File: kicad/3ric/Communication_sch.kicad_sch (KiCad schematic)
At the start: 15 parts, among them J4_ACIA 6502-library_65C51N

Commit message: cleaning up of the schematic
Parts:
- H1_LEVEL_SHIFT1: renamed from H1_LEVEL_SHIFT; footprint (none) -> Package_SO:ETSSOP-20-1EP_4.4x6.5mm_P0.65mm_EP3x4.2mm
- Y_SNES_1, Y_SNES_2: footprint Nintendo:SNES_Controller_Socket -> snes:SNES_Controller_Socket
- renumbered H2_ACIA_CLK to H2_ACIA_CLK1, I1_VIA to I1_VIA1, J4_ACIA to J4_ACIA1, RM to RM1, Y_DEVICE_PORT to Y_DEVICE_PORT1, Y_MICRO_SD to Y_MICRO_SD1, Y_PS2_KB to Y_PS2_KB1, Y_PS2_MOUSE to Y_PS2_MOUSE1, Y_SERIAL_PINS to Y_SERIAL_PINS1
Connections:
- net V3.3 is gone; now on net 3.3V: Y_DEVICE_PORT1.20 (Pin_20)
- net ~{CS_IO6} is gone; now on net R~{W}: Y_DEVICE_PORT1.22 (Pin_22)
- net GND: no longer J4_ACIA1.9 (~{CTS})
- net ~{CTS}: now also J4_ACIA1.9 (~{CTS})
- net ~{RTS}: now also J4_ACIA1.8 (~{RTS})
- net VIA1_PA5: no longer names the net of I1_VIA1.7 (PA5)
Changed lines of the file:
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@@
 	)
 	(no_connect
+		(at 139.7 63.5)
+	)
+	(no_connect
 		(at 41.91 115.57)
 	)
@@
 	)
 	(no_connect
-		(at 67.31 125.73)
-	)
-	(no_connect
 		(at 97.79 68.58)
 	)
@@
 		)
 	)
+	(global_label "R~{W}"
+		(shape input)
+		(at 124.46 142.24 0)
+		(fields_autoplaced yes)
+		(effects
+			(font
+				(size 1.27 1.27)
+			)
+			(justify left)
+		)
+		(property "Intersheetrefs" "${INTERSHEET_REFS}"
+			(at 154.94 252.73 0)
+			(effects
+				(font
+					(size 1.27 1.27)
+				)
+				(justify right)
+				(hide yes)
+			)
+		)
+	)
 	(global_label "CA0"
 		(shape input)
@@
 		)
 	)
-	(global_label "GND"
-		(shape input)
-		(at 67.31 123.19 0)
-		(fields_autoplaced yes)
-		(effects
-			(font
-				(size 0.9906 0.9906)
-			)
-			(justify left)
-		)
-		(property "Intersheetrefs" "${INTERSHEET_REFS}"
-			(at -53.34 46.99 0)
-			(effects
-				(font
-					(size 1.27 1.27)
-				)
-				(hide yes)
-			)
-		)
-	)
 	(global_label "~{IRQ_VIA1}"
 		(shape input)
@@
 		)
 	)
-	(global_label "~{CS_IO6}"
-		(shape input)
-		(at 124.46 142.24 0)
-		(fields_autoplaced yes)
-		(effects
-			(font
-				(size 1.27 1.27)
-			)
-			(justify left)
-		)
-		(property "Intersheetrefs" "${INTERSHEET_REFS}"
-			(at 134.0371 142.24 0)
-			(effects
-				(font
-					(size 1.27 1.27)
-				)
-				(justify left)
-				(hide yes)
-			)
-		)
-	)
 	(global_label "CLK_MOUSE"
 		(shape output)
@@
 		)
 	)
+	(global_label "3.3V"
+		(shape input)
+		(at 124.46 139.7 0)
+		(fields_autoplaced yes)
+		(effects
+			(font
+				(size 0.9906 0.9906)
+			)
+			(justify left)
+		)
+		(property "Intersheetrefs" "${INTERSHEET_REFS}"
+			(at 129.5498 139.6381 0)
+			(effects
+				(font
+					(size 0.9906 0.9906)
+				)
+				(justify left)
+				(hide yes)
+			)
+		)
+	)
 	(global_label "DATA_MOUSE"
 		(shape output)
@@
 		)
 	)
-	(global_label "V3.3"
-		(shape input)
-		(at 124.46 139.7 0)
-		(fields_autoplaced yes)
-		(effects
-			(font
-				(size 0.9906 0.9906)
-			)
-			(justify left)
-		)
-		(property "Intersheetrefs" "${INTERSHEET_REFS}"
-			(at 129.5498 139.6381 0)
-			(effects
-				(font
-					(size 0.9906 0.9906)
-				)
-				(justify left)
-				(hide yes)
-			)
-		)
-	)
 	(global_label "CA7"
 		(shape input)
@@
 		)
 	)
+	(global_label "~{RTS}"
+		(shape input)
+		(at 67.31 125.73 0)
+		(fields_autoplaced yes)
+		(effects
+			(font
+				(size 0.9906 0.9906)
+			)
+			(justify left)
+		)
+		(property "Intersheetrefs" "${INTERSHEET_REFS}"
+			(at 196.85 2.54 0)
+			(effects
+				(font
+					(size 1.27 1.27)
+				)
+				(justify left)
+				(hide yes)
+			)
+		)
+	)
 	(global_label "CD2"
 		(shape input)
@@
 		)
 	)
+	(global_label "~{CTS}"
+		(shape input)
+		(at 67.31 123.19 0)
+		(fields_autoplaced yes)
+		(effects
+			(font
+				(size 0.9906 0.9906)
+			)
+			(justify left)
+		)
+		(property "Intersheetrefs" "${INTERSHEET_REFS}"
+			(at -74.93 0 0)
+			(effects
+				(font
+					(size 1.27 1.27)
+				)
+				(hide yes)
+			)
+		)
+	)
 	(global_label "CD3"
 		(shape input)
@@
 		)
 	)
-	(global_label "VIA1_PA5"
-		(shape input)
-		(at 139.7 63.5 180)
-		(fields_autoplaced yes)
-		(effects
-			(font
-				(size 0.9906 0.9906)
-			)
-			(justify right)
-		)
-		(property "Intersheetrefs" "${INTERSHEET_REFS}"
-			(at -20.32 -26.67 0)
-			(effects
-				(font
-					(size 1.27 1.27)
-				)
-				(hide yes)
-			)
-		)
-	)
 	(global_label "CA2"
 		(shape input)
@@
 		(on_board yes)
 		(dnp no)
-		(property "Reference" "Y_PS2_KB"
+		(property "Reference" "Y_PS2_KB1"
 			(at 227.33 37.6682 0)
 			(effects
@@
 			(project "3ric"
 				(path "/e63e39d7-6ac0-4ffd-8aa3-1841a4541b55/817a35a7-de63-4412-ae79-57fde5eabc67"
-					(reference "Y_PS2_KB")
+					(reference "Y_PS2_KB1")
 					(unit 1)
 				)
@@
 		(dnp no)
 		(fields_autoplaced yes)
-		(property "Reference" "Y_MICRO_SD"
+		(property "Reference" "Y_MICRO_SD1"
 			(at 51.435 40.7502 0)
 			(effects
@@
 			(project "3ric"
 				(path "/e63e39d7-6ac0-4ffd-8aa3-1841a4541b55/817a35a7-de63-4412-ae79-57fde5eabc67"
-					(reference "Y_MICRO_SD")
+					(reference "Y_MICRO_SD1")
 					(unit 1)
 				)
@@
 		(on_board yes)
 		(dnp no)
-		(property "Reference" "Y_PS2_MOUSE"
+		(property "Reference" "Y_PS2_MOUSE1"
 			(at 227.33 80.8482 0)
 			(effects
@@
 			(project "3ric"
 				(path "/e63e39d7-6ac0-4ffd-8aa3-1841a4541b55/817a35a7-de63-4412-ae79-57fde5eabc67"
-					(reference "Y_PS2_MOUSE")
+					(reference "Y_PS2_MOUSE1")
 					(unit 1)
 				)
@@
 		(on_board yes)
 		(dnp no)
-		(property "Reference" "Y_DEVICE_PORT"
+		(property "Reference" "Y_DEVICE_PORT1"
 			(at 118.11 111.3282 0)
 			(effects
@@
 			(project "3ric"
 				(path "/e63e39d7-6ac0-4ffd-8aa3-1841a4541b55/817a35a7-de63-4412-ae79-57fde5eabc67"
-					(reference "Y_DEVICE_PORT")
+					(reference "Y_DEVICE_PORT1")
 					(unit 1)
 				)
@@
 		(on_board yes)
 		(dnp no)
-		(property "Reference" "H2_ACIA_CLK"
+		(property "Reference" "H2_ACIA_CLK1"
 			(at 50.9524 163.9316 0)
 			(effects
@@
 			(project "3ric"
 				(path "/e63e39d7-6ac0-4ffd-8aa3-1841a4541b55/817a35a7-de63-4412-ae79-57fde5eabc67"
-					(reference "H2_ACIA_CLK")
+					(reference "H2_ACIA_CLK1")
 					(unit 1)
 				)
@@
 		(on_board yes)
 		(dnp no)
-		(property "Reference" "I1_VIA"
+		(property "Reference" "I1_VIA1"
 			(at 152.4 41.529 0)
 			(effects
@@
 			(project "3ric"
 				(path "/e63e39d7-6ac0-4ffd-8aa3-1841a4541b55/817a35a7-de63-4412-ae79-57fde5eabc67"
-					(reference "I1_VIA")
+					(reference "I1_VIA1")
 					(unit 1)
 				)
@@
 		(on_board yes)
 		(dnp no)
-		(property "Reference" "Y_SERIAL_PINS"
+		(property "Reference" "Y_SERIAL_PINS1"
 			(at 152.4 181.1782 0)
 			(effects
@@
 			(project "3ric"
 				(path "/e63e39d7-6ac0-4ffd-8aa3-1841a4541b55/817a35a7-de63-4412-ae79-57fde5eabc67"
-					(reference "Y_SERIAL_PINS")
+					(reference "Y_SERIAL_PINS1")
 					(unit 1)
 				)
@@
 		(on_board yes)
 		(dnp no)
-		(property "Reference" "H1_LEVEL_SHIFT"
+		(property "Reference" "H1_LEVEL_SHIFT1"
 			(at 107.696 36.068 0)
 			(effects
@@
 			)
 		)
-		(property "Footprint" ""
+		(property "Footprint" "Package_SO:ETSSOP-20-1EP_4.4x6.5mm_P0.65mm_EP3x4.2mm"
 			(at 107.95 80.01 0)
 			(effects
@@
 			(project "3ric"
 				(path "/e63e39d7-6ac0-4ffd-8aa3-1841a4541b55/817a35a7-de63-4412-ae79-57fde5eabc67"
-					(reference "H1_LEVEL_SHIFT")
+					(reference "H1_LEVEL_SHIFT1")
 					(unit 1)
 				)
@@
 			)
 		)
-		(property "Footprint" "Nintendo:SNES_Controller_Socket"
+		(property "Footprint" "snes:SNES_Controller_Socket"
 			(at 194.31 142.24 0)
 			(effects
@@
 			)
 		)
-		(property "Footprint" "Nintendo:SNES_Controller_Socket"
+		(property "Footprint" "snes:SNES_Controller_Socket"
 			(at 242.57 140.97 0)
 			(effects
@@
 		(on_board yes)
 		(dnp no)
-		(property "Reference" "RM"
+		(property "Reference" "RM1"
 			(at 240.538 82.6516 0)
 			(effects
@@
 			(project "3ric"
 				(path "/e63e39d7-6ac0-4ffd-8aa3-1841a4541b55/817a35a7-de63-4412-ae79-57fde5eabc67"
-					(reference "RM")
+					(reference "RM1")
 					(unit 1)
 				)
@@
 		(dnp no)
 		(fields_autoplaced yes)
-		(property "Reference" "J4_ACIA"
+		(property "Reference" "J4_ACIA1"
 			(at 54.61 104.3772 0)
 			(effects
@@
 			(project "3ric"
 				(path "/e63e39d7-6ac0-4ffd-8aa3-1841a4541b55/817a35a7-de63-4412-ae79-57fde5eabc67"
-					(reference "J4_ACIA")
+					(reference "J4_ACIA1")
 					(unit 1)
 				)

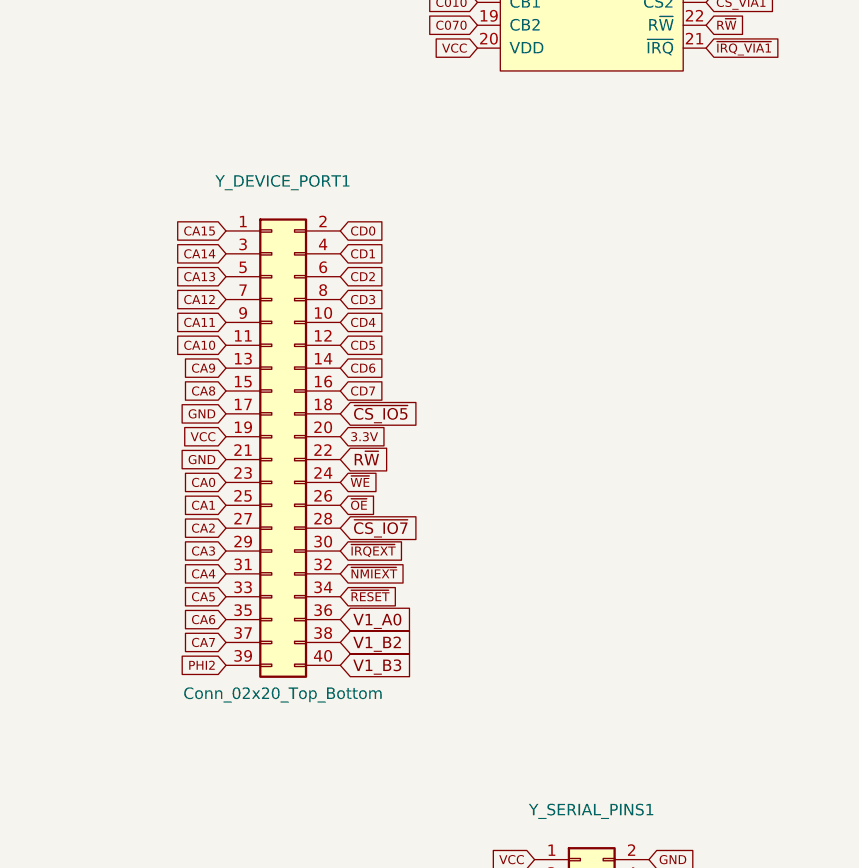
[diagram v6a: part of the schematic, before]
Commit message: updated schematics and PCB PNG of the breadboard layout
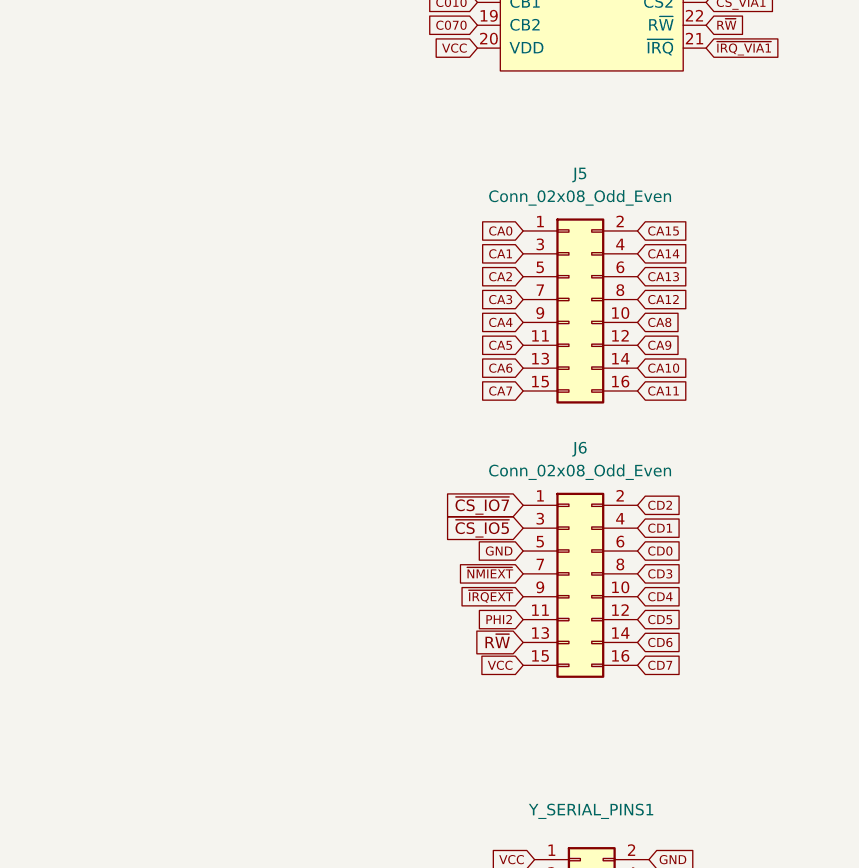
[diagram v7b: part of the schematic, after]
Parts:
- removed Y_DEVICE_PORT1: Conn_02x20_Top_Bottom, Connector_IDC:IDC-Header_2x20_P2.54mm_Vertical, symbol Connector_Generic:Conn_02x20_Odd_Even
- added J5, J6: Conn_02x08_Odd_Even, Connector_PinHeader_2.54mm:PinHeader_2x08_P2.54mm_Vertical, symbol Connector_Generic:Conn_02x08_Odd_Even
- RKB1, RKB2, RM1, RM2: footprint Resistor_THT:R_Axial_DIN0207_L6.3mm_D2.5mm_P7.62mm_Horizontal -> Resistor_SMD:R_0805_2012Metric_Pad1.20x1.40mm_HandSolder
- Y_MICRO_SD1: footprint badger6502pico:microSD_Amazon2 -> sdcard:microSD_Amazon2
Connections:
- net CA0: now also J5.1 (Pin_1)
- net CA1: now also J5.3 (Pin_3)
- net CA10: now also J5.14 (Pin_14)
- net CA11: now also J5.16 (Pin_16)
- net CA12: now also J5.8 (Pin_8)
- net CA13: now also J5.6 (Pin_6)
- net CA14: now also J5.4 (Pin_4)
- net CA15: now also J5.2 (Pin_2)
- net CA2: now also J5.5 (Pin_5)
- net CA3: now also J5.7 (Pin_7)
- net CA4: now also J5.9 (Pin_9)
- net CA5: now also J5.11 (Pin_11)
- net CA6: now also J5.13 (Pin_13)
- net CA7: now also J5.15 (Pin_15)
- net CA8: now also J5.10 (Pin_10)
- net CA9: now also J5.12 (Pin_12)
- net CD0: now also J6.6 (Pin_6)
- net CD1: now also J6.4 (Pin_4)
- net CD2: now also J6.2 (Pin_2)
- net CD3: now also J6.8 (Pin_8)
- net CD4: now also J6.10 (Pin_10)
- net CD5: now also J6.12 (Pin_12)
- net CD6: now also J6.14 (Pin_14)
- net CD7: now also J6.16 (Pin_16)
- net GND: now also J6.5 (Pin_5)
- net PHI2: now also J6.11 (Pin_11)
- net R~{W}: now also J6.13 (Pin_13)
- net VCC: now also J6.15 (Pin_15)
- net ~{CS_IO5}: now also J6.3 (Pin_3)
- net ~{CS_IO7}: now also J6.1 (Pin_1)
- net ~{IRQEXT}: now also J6.9 (Pin_9)
- net ~{NMIEXT}: now also J6.7 (Pin_7)

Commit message: pcb layout continued
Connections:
- net CA10: now also J5.6 (Pin_6); no longer J5.14 (Pin_14)
- net CA11: now also J5.8 (Pin_8); no longer J5.16 (Pin_16)
- net CA12: now also J5.10 (Pin_10); no longer J5.8 (Pin_8)
- net CA13: now also J5.12 (Pin_12); no longer J5.6 (Pin_6)
- net CA14: now also J5.14 (Pin_14); no longer J5.4 (Pin_4)
- net CA15: now also J5.16 (Pin_16); no longer J5.2 (Pin_2)
- net CA8: now also J5.2 (Pin_2); no longer J5.10 (Pin_10)
- net CA9: now also J5.4 (Pin_4); no longer J5.12 (Pin_12)
- net CD0: now also J6.2 (Pin_2); no longer J6.6 (Pin_6)
- net CD2: now also J6.6 (Pin_6); no longer J6.2 (Pin_2)
- net GND: now also J4_ACIA1.9 (~{CTS}), J6.1 (Pin_1); no longer J6.5 (Pin_5)
- net ~{CS_IO5}: now also J6.5 (Pin_5); no longer J6.3 (Pin_3)
- net ~{CS_IO7}: now also J6.3 (Pin_3); no longer J6.1 (Pin_1)
- net at Y_MICRO_SD1.2 (DAT3/CD): now also H1_LEVEL_SHIFT1.1 (A1); no longer H1_LEVEL_SHIFT1.5 (A4)
- net at Y_MICRO_SD1.3 (CMD): now also H1_LEVEL_SHIFT1.4 (A3); no longer H1_LEVEL_SHIFT1.3 (A2)
- net at Y_MICRO_SD1.5 (CLK): now also H1_LEVEL_SHIFT1.3 (A2); no longer H1_LEVEL_SHIFT1.4 (A3)
- net at Y_MICRO_SD1.7 (DAT0): now also H1_LEVEL_SHIFT1.5 (A4); no longer H1_LEVEL_SHIFT1.1 (A1)
- net at I1_VIA1.3 (PA1): now also H1_LEVEL_SHIFT1.16 (B4); no longer H1_LEVEL_SHIFT1.20 (B1)
- net at I1_VIA1.4 (PA2): now also H1_LEVEL_SHIFT1.17 (B3); no longer H1_LEVEL_SHIFT1.18 (B2)
- net at I1_VIA1.5 (PA3): now also H1_LEVEL_SHIFT1.18 (B2); no longer H1_LEVEL_SHIFT1.17 (B3)
- net at I1_VIA1.6 (PA4): now also H1_LEVEL_SHIFT1.20 (B1); no longer H1_LEVEL_SHIFT1.16 (B4)
- net V1_A0: no longer names the net of I1_VIA1.2 (PA0)
- net V1_B2: no longer names the net of I1_VIA1.12 (PB2)
- net V1_B3: no longer names the net of I1_VIA1.13 (PB3)
- net ~{CTS}: no longer names the net of Y_SERIAL_PINS1.4 (Pin_4)
- net ~{CTS}: no longer J4_ACIA1.9 (~{CTS})
- net ~{RTS}: no longer names the net of Y_SERIAL_PINS1.3 (Pin_3)
- net ~{RTS}: no longer J4_ACIA1.8 (~{RTS})
- no-connect marks 20 -> 26
